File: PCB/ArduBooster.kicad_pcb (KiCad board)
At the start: 2 copper layers, 70.1 x 55.1 mm, 35 parts, among them IC1 ATMEGA328-P, P1 ISP, P2 DEBUG TX/RX, P3 CONTROL, P4 MAIN_CONN, U1 ICL7660, U2 LM358, U3 4052, X1 CRYSTAL

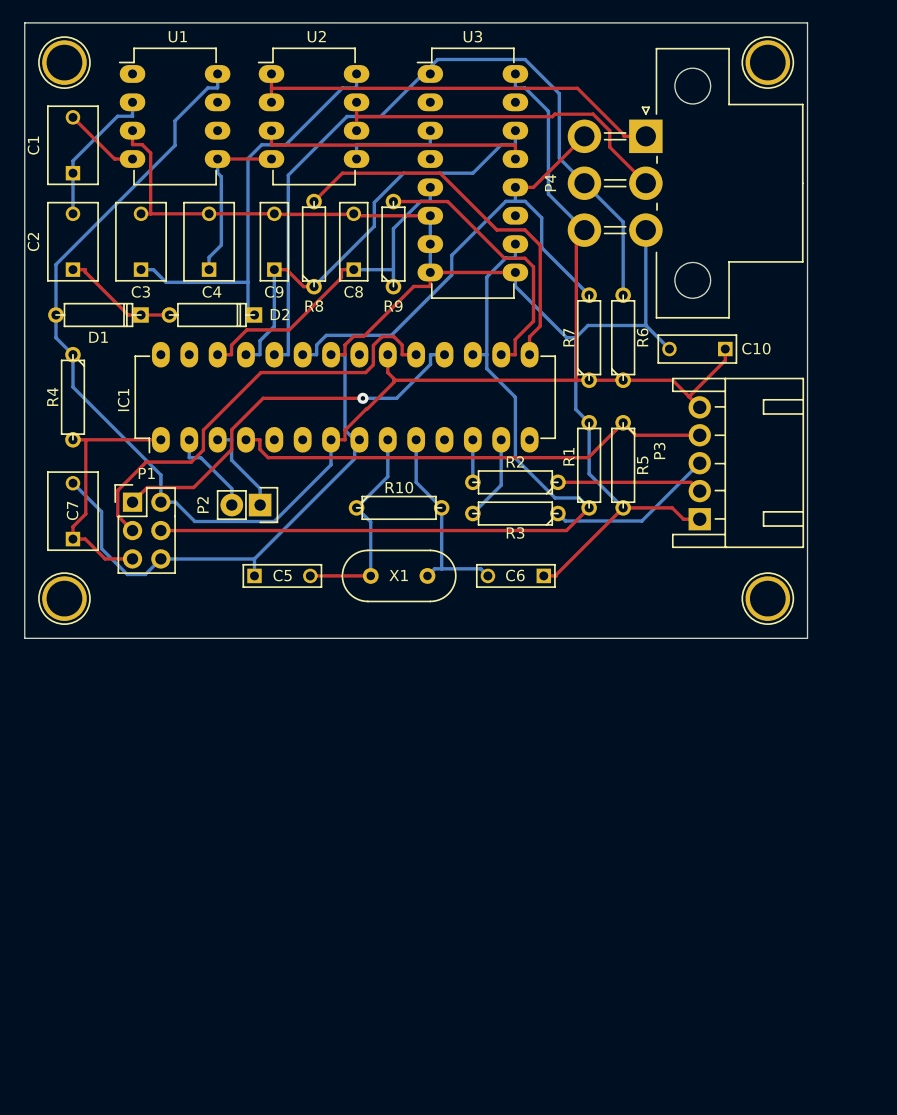
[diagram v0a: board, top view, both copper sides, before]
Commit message: New route, gerber files and drill files.
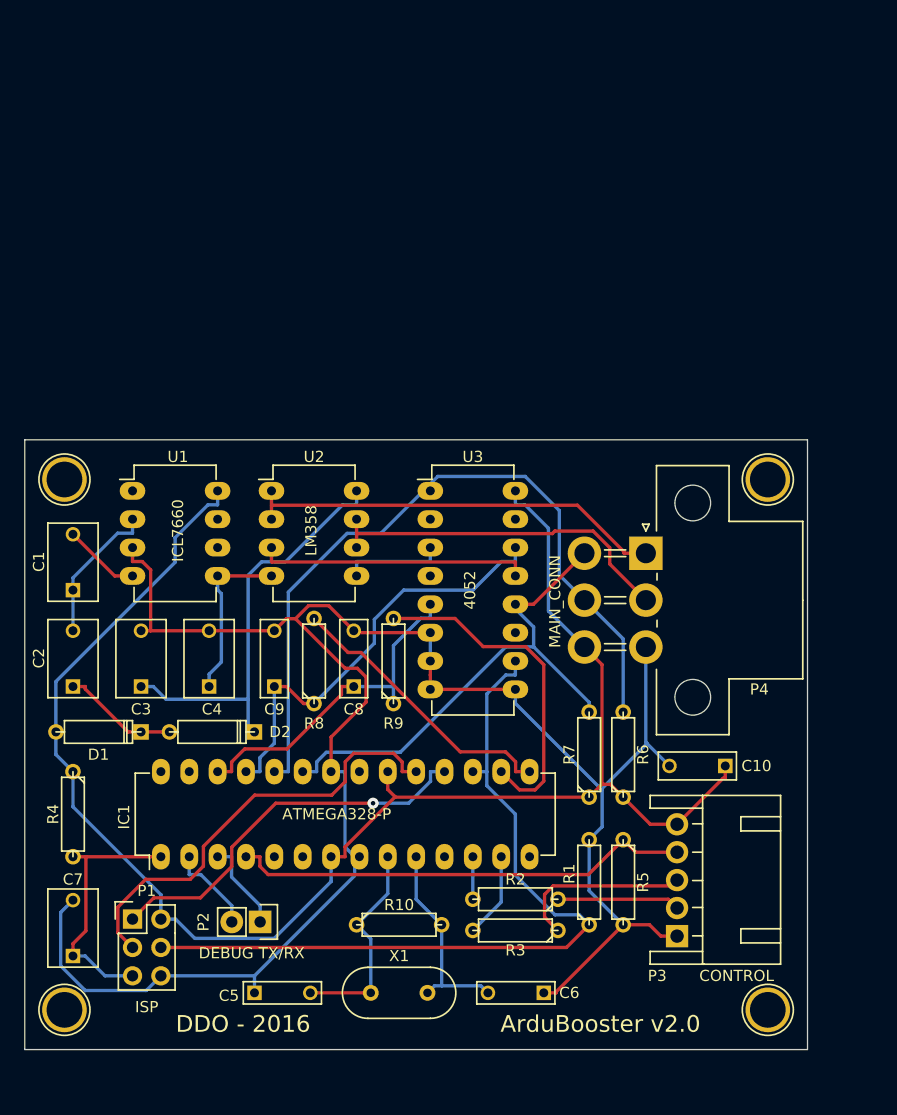
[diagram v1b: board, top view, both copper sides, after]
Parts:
- moved P3 37.4 mm to (168.9, 118.6)
- moved C2 37.3 mm to (114.8, 96.3)
- moved C3 37.3 mm to (120.9, 96.3)
- moved C4 37.3 mm to (127.0, 96.3)
- moved C8 37.3 mm to (140.0, 96.3)
- moved C9 37.3 mm to (132.8, 96.3)
- moved R1 37.3 mm to (161.0, 113.8)
- moved R10 37.3 mm to (144.0, 117.6)
- moved R2 37.3 mm to (154.4, 115.3)
- moved R5 37.3 mm to (164.1, 113.8)
- moved D1 37.3 mm to (117.1, 100.3)
- moved D2 37.3 mm to (127.3, 100.3)
- moved H1 37.3 mm to (177.0, 77.7)
- moved H3 37.3 mm to (114.0, 77.7)
- moved P4 37.3 mm to (166.1, 84.3)
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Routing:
- net Net-(IC1-Pad15): track 34.2 -> 25.5 mm
- net GNDREF: track 169.0 -> 176.4 mm
- net Net-(IC1-Pad16): track 24.8 -> 30.4 mm
- net /Base Arduino/LED1: track 13.0 -> 11.0 mm
- net /Base Arduino/SWITCH: track 43.6 -> 41.5 mm
- net /Base Arduino/LED2: track 15.1 -> 16.1 mm
- net /Base Arduino/CH0_PEDAL_SIG: track 47.2 -> 46.3 mm
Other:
- board size 70.1 x 55.1 mm -> 70.1 x 54.6 mm
- board text added: "ArduBooster v2.0"
- board text added: "DDO - 2016"
- board text added: "www.github.com/ddo02/ArduBooster"

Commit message: Output feedback connection  correction.
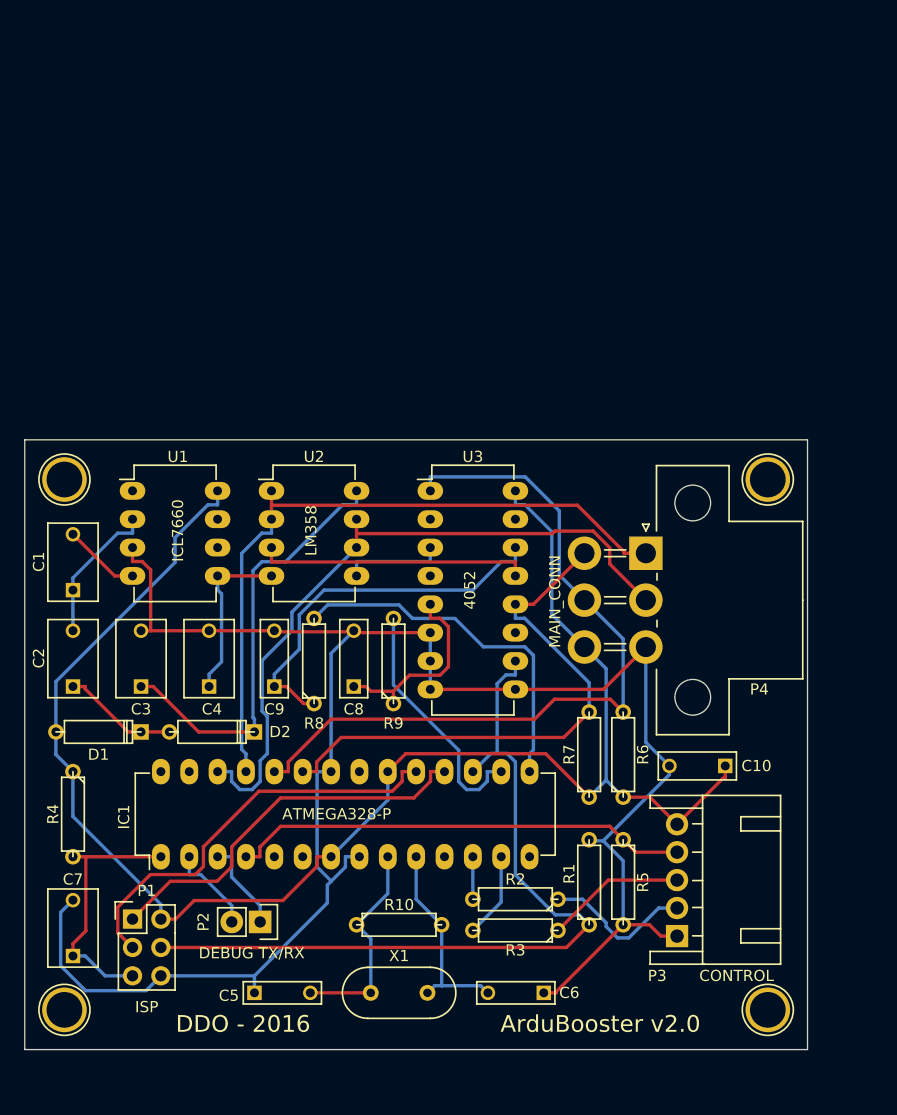
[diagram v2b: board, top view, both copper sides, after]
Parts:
- C10: value 100n -> 100nF
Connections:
- IC1 pad 25: /Base Arduino/CH0_ARDUINO_SIG -> /Base Arduino/CH0_OUT
- IC1 pad 26: /Base Arduino/CH1_ARDUINO_SIG -> /Base Arduino/CH1_OUT
- P4 pad 1: /Connectors/CH0_OUT -> /Base Arduino/CH0_OUT
- P4 pad 2: /Connectors/CH1_OUT -> /Base Arduino/CH1_OUT
- U2 pad 1: /Connectors/CH0_OUT -> /Base Arduino/CH0_OUT
- U2 pad 2: /Connectors/CH0_OUT -> /Base Arduino/CH0_OUT
- U2 pad 6: /Connectors/CH1_OUT -> /Base Arduino/CH1_OUT
- U2 pad 7: /Connectors/CH1_OUT -> /Base Arduino/CH1_OUT
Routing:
- net /Base Arduino/CH0_OUT: track 0.00 -> 62.3 mm
- net /Base Arduino/CH1_OUT: track 0.00 -> 62.2 mm
- net /Connectors/CH0_OUT: track 37.9 -> 0.00 mm
- net /Connectors/CH1_OUT: track 32.0 -> 0.00 mm
- net /Base Arduino/CH1_ARDUINO_SIG: track 30.6 -> 17.4 mm
- net Net-(IC1-Pad16): track 30.4 -> 22.3 mm
- net Net-(IC1-Pad15): track 25.5 -> 32.6 mm
- net /Base Arduino/CH0_ARDUINO_SIG: track 39.4 -> 34.1 mm
- net /Base Arduino/LED2: track 16.1 -> 12.5 mm
- net GNDREF: track 176.4 -> 172.9 mm
- net /Base Arduino/CH0_PEDAL_SIG: track 46.3 -> 49.3 mm
- net /Base Arduino/LED1: track 11.0 -> 13.4 mm
- net /Base Arduino/SCK: track 39.8 -> 37.4 mm
- net /Base Arduino/MOSI: track 70.7 -> 72.0 mm
- net /Base Arduino/CH1_PEDAL_SIG: track 68.2 -> 69.4 mm
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
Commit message: Last commit before Mux/Demux removel. Single layer PCB incompete (3 wires). Add ADC input filter.
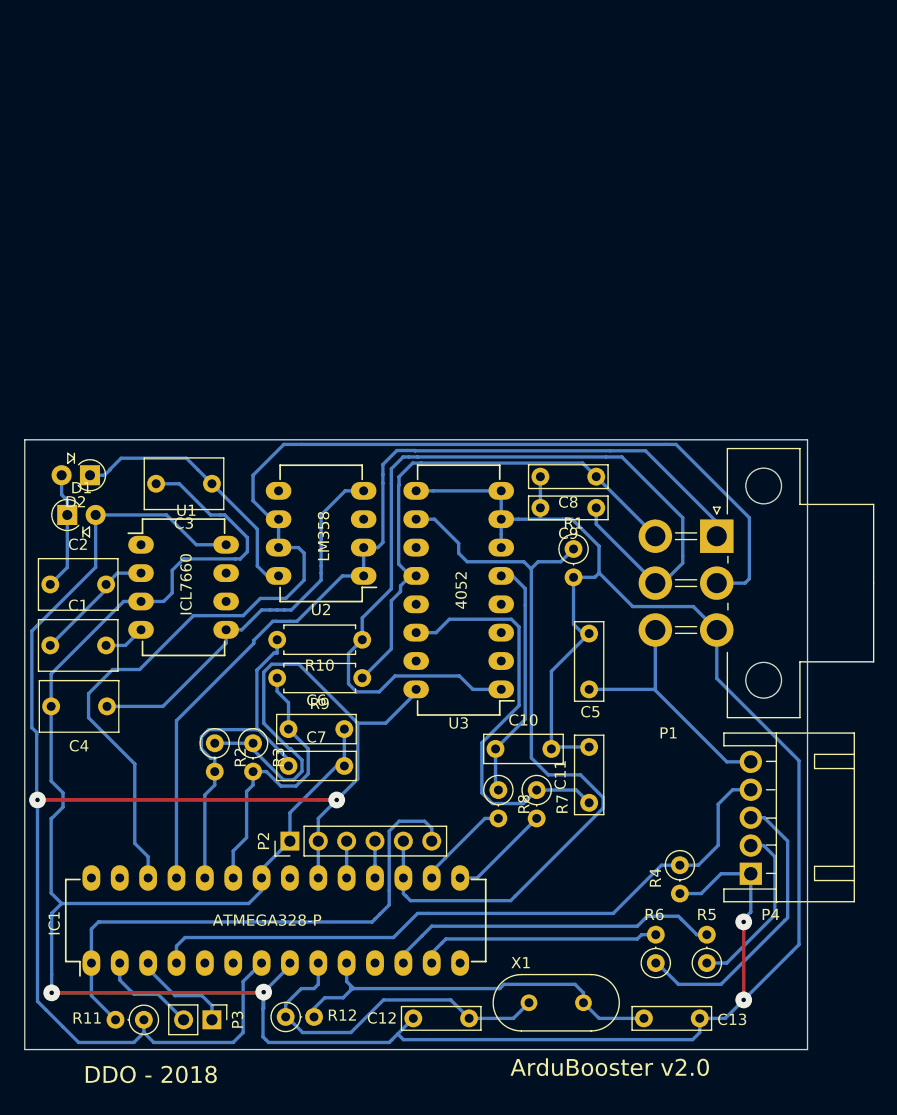
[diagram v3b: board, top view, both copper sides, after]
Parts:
- removed H1, H2, H3, H4: , Connect:1pin
- added C11: 100n, Capacitors_THT:C_Rect_L7.0mm_W2.5mm_P5.00mm, F.Cu at (161.0, 106.7)
- added C12: 22p, Capacitors_THT:C_Rect_L7.0mm_W2.0mm_P5.00mm, F.Cu at (145.3, 126.0)
- added C13: 22p, Capacitors_THT:C_Rect_L7.0mm_W2.0mm_P5.00mm, F.Cu at (170.9, 126.0)
- added R11: 10k, Resistors_THT:R_Axial_DIN0207_L6.3mm_D2.5mm_P2.54mm_Vertical, F.Cu at (121.2, 126.1)
- added R12: 1M, Resistors_THT:R_Axial_DIN0207_L6.3mm_D2.5mm_P2.54mm_Vertical, F.Cu at (133.9, 125.9)
- C1, C2, C3, C4: footprint Capacitors_ThroughHole:C_Rect_L7_W4.5_P5 -> Capacitors_THT:C_Rect_L7.0mm_W4.5mm_P5.00mm
- C10: value 100nF -> 100n; footprint Capacitors_ThroughHole:C_Rect_L7_W2.5_P5 -> Capacitors_THT:C_Rect_L7.0mm_W2.5mm_P5.00mm
- C5: value 22p -> 100nF; footprint Capacitors_ThroughHole:C_Rect_L7_W2_P5 -> Capacitors_THT:C_Rect_L7.0mm_W2.5mm_P5.00mm
- C6: value 22p -> 100n; footprint Capacitors_ThroughHole:C_Rect_L7_W2_P5 -> Capacitors_THT:C_Rect_L7.0mm_W2.5mm_P5.00mm
- C7: value 1u -> 100n; footprint Capacitors_ThroughHole:C_Rect_L7_W4.5_P5 -> Capacitors_THT:C_Rect_L7.0mm_W2.5mm_P5.00mm
- C8, C9: value 100n -> 1n; footprint Capacitors_ThroughHole:C_Rect_L7_W2.5_P5 -> Capacitors_THT:C_Rect_L7.0mm_W2.0mm_P5.00mm
- D1, D2: footprint Discret:D3 -> Diodes_THT:D_A-405_P2.54mm_Vertical_AnodeUp
- P1: value ISP -> MAIN_CONN; footprint Pin_Headers:Pin_Header_Straight_2x03 -> Connectors_Molex:Molex_MiniFit-JR-5569-06A1_2x03x4.20mm_Angled
- P2: value DEBUG TX/RX -> ISP; footprint Pin_Headers:Pin_Header_Straight_1x02 -> Pin_Headers:Pin_Header_Straight_1x06_Pitch2.54mm
- P3: value CONTROL -> DEBUG TX/RX; footprint Connect:Wafer_Horizontal15x5.8x7RM2.5-5 -> Pin_Headers:Pin_Header_Straight_1x02_Pitch2.54mm
- P4: value MAIN_CONN -> CONTROL; footprint Connectors_Molex:Molex_MiniFit-JR-5569-06A1_2x03x4.20mm_Angled -> Connectors:Wafer_Horizontal15x5.8x7RM2.5-5
- R1, R4: footprint Discret:R3 -> Resistors_THT:R_Axial_DIN0207_L6.3mm_D2.5mm_P2.54mm_Vertical
- R10: value 1M -> 2.2k; footprint Discret:R3 -> Resistors_THT:R_Axial_DIN0207_L6.3mm_D2.5mm_P7.62mm_Horizontal
- R2, R3: value 470 -> 10k; footprint Discret:R3 -> Resistors_THT:R_Axial_DIN0207_L6.3mm_D2.5mm_P2.54mm_Vertical
- R5, R6: value 10k -> 470; footprint Discret:R3 -> Resistors_THT:R_Axial_DIN0207_L6.3mm_D2.5mm_P2.54mm_Vertical
- R7, R8: value 10k -> 100k; footprint Discret:R3 -> Resistors_THT:R_Axial_DIN0207_L6.3mm_D2.5mm_P2.54mm_Vertical
- R9: value 10k -> 2.2k; footprint Discret:R3 -> Resistors_THT:R_Axial_DIN0207_L6.3mm_D2.5mm_P7.62mm_Horizontal
- X1: footprint Crystals:HC-49V -> Crystals:Crystal_HC49-U_Vertical
- moved P1 62.6 mm to (172.5, 82.8), turned to 270 degrees
- moved R4 54.5 mm to (169.2, 112.3)
- moved P3 42.3 mm to (127.3, 126.1), turned to 270 degrees
- moved C5 40.5 mm to (161.0, 96.5), turned to 90 degrees
- moved C9 33.0 mm to (161.7, 80.3), turned to 180 degrees
- moved C6 32.9 mm to (134.1, 100.1), turned to 0 degrees
- moved R2 30.3 mm to (127.5, 101.3), turned to 270 degrees
- moved P4 30.2 mm to (175.5, 113.0), turned to 90 degrees
- moved R1 29.9 mm to (159.6, 83.9), turned to 270 degrees
- moved R3 28.9 mm to (130.9, 101.3), turned to 270 degrees
- moved C8 28.7 mm to (161.7, 77.5), turned to 180 degrees
- moved R10 25.7 mm to (140.7, 92.1), turned to 180 degrees
- moved C7 25.7 mm to (134.1, 103.4), turned to 0 degrees
- moved D2 25.4 mm to (116.3, 77.3), turned to 180 degrees
- moved C10 20.6 mm to (152.7, 101.9), turned to 0 degrees
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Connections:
- C10 pad 1: +5V -> /Base Arduino/CH1_ARDUINO_SIG
- C5 pad 1: GNDREF -> +5V
- C5 pad 2: Net-(C5-Pad2) -> GNDREF
- C6 pad 1: GNDREF -> Net-(C6-Pad1)
- C6 pad 2: Net-(C6-Pad2) -> GNDREF
- C7 pad 1: /Base Arduino/RESET -> Net-(C7-Pad1)
- C8 pad 1: /Base Arduino/CH1_ARDUINO_SIG -> /Base Arduino/CH0_PEDAL_SIG
- C9 pad 1: /Base Arduino/CH0_ARDUINO_SIG -> /Base Arduino/CH1_PEDAL_SIG
- IC1 pad 10: Net-(C6-Pad2) -> Net-(C13-Pad2)
- IC1 pad 11: Net-(IC1-Pad11) -> (no net)
- IC1 pad 14: Net-(IC1-Pad14) -> (no net)
- IC1 pad 21: Net-(IC1-Pad21) -> (no net)
- IC1 pad 23: /Base Arduino/CH0_PEDAL_SIG -> Net-(C6-Pad1)
- IC1 pad 24: /Base Arduino/CH1_PEDAL_SIG -> Net-(C7-Pad1)
- IC1 pad 27: Net-(IC1-Pad27) -> (no net)
- IC1 pad 28: Net-(IC1-Pad28) -> (no net)
- IC1 pad 5: Net-(IC1-Pad5) -> (no net)
- IC1 pad 6: Net-(IC1-Pad6) -> (no net)
- IC1 pad 9: Net-(C5-Pad2) -> Net-(C12-Pad2)
- P1 pad 1: /Base Arduino/MISO -> /Base Arduino/CH0_OUT
- P1 pad 2: +5V -> /Base Arduino/CH1_OUT
- P1 pad 3: /Base Arduino/SCK -> GNDREF
- P1 pad 4: /Base Arduino/MOSI -> /Base Arduino/CH0_PEDAL_SIG
- P1 pad 5: /Base Arduino/RESET -> /Base Arduino/CH1_PEDAL_SIG
- P1 pad 6: GNDREF -> +5V
- P2 pad 1: /Base Arduino/TX -> GNDREF
- P2 pad 2: /Base Arduino/RX -> +5V
- P3 pad 1: GNDREF -> /Base Arduino/TX
- P3 pad 2: /Base Arduino/LED1 -> /Base Arduino/RX
- P4 pad 1: /Base Arduino/CH0_OUT -> GNDREF
- P4 pad 2: /Base Arduino/CH1_OUT -> /Base Arduino/LED1
- P4 pad 3: GNDREF -> /Base Arduino/LED2
- P4 pad 4: /Base Arduino/CH0_PEDAL_SIG -> /Base Arduino/SWITCH
- P4 pad 5: /Base Arduino/CH1_PEDAL_SIG -> +5V
- R10 pad 1: Net-(C5-Pad2) -> /Base Arduino/CH1_PEDAL_SIG
- R10 pad 2: Net-(C6-Pad2) -> Net-(C7-Pad1)
- R2 pad 1: /Base Arduino/LED1 -> +5V
- R2 pad 2: Net-(IC1-Pad12) -> Net-(C7-Pad1)
- R3 pad 1: /Base Arduino/LED2 -> +5V
- R3 pad 2: Net-(IC1-Pad13) -> Net-(C6-Pad1)
- R4 pad 1: +5V -> /Base Arduino/SWITCH
- R4 pad 2: /Base Arduino/RESET -> GNDREF
- R5 pad 1: /Base Arduino/SWITCH -> /Base Arduino/LED1
- R5 pad 2: GNDREF -> Net-(IC1-Pad12)
- R6 pad 1: +5V -> /Base Arduino/LED2
- R6 pad 2: /Base Arduino/CH1_PEDAL_SIG -> Net-(IC1-Pad13)
- R7 pad 1: +5V -> /Base Arduino/CH0_ARDUINO_SIG
- R7 pad 2: /Base Arduino/CH0_PEDAL_SIG -> Net-(IC1-Pad15)
- R8 pad 1: /Base Arduino/CH0_ARDUINO_SIG -> /Base Arduino/CH1_ARDUINO_SIG
- R8 pad 2: Net-(IC1-Pad15) -> Net-(IC1-Pad16)
- R9 pad 1: /Base Arduino/CH1_ARDUINO_SIG -> /Base Arduino/CH0_PEDAL_SIG
- R9 pad 2: Net-(IC1-Pad16) -> Net-(C6-Pad1)
- U1 pad 6: Net-(U1-Pad6) -> (no net)
- U1 pad 7: Net-(U1-Pad7) -> (no net)
- U3 pad 11: Net-(U3-Pad11) -> (no net)
- U3 pad 15: Net-(U3-Pad15) -> (no net)
- U3 pad 2: Net-(U3-Pad2) -> (no net)
- U3 pad 4: Net-(U3-Pad4) -> (no net)
- X1 pad 1: Net-(C6-Pad2) -> Net-(C13-Pad2)
- X1 pad 2: Net-(C5-Pad2) -> Net-(C12-Pad2)
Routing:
- net GNDREF: track 172.9 -> 299.8 mm, vias 0 -> 4
- net /Base Arduino/CH1_OUT: track 62.2 -> 111.8 mm
- net +5V: track 143.9 -> 190.6 mm, vias 0 -> 2
- net Net-(C13-Pad2): track 0.00 -> 36.1 mm
- net /Base Arduino/SCK: track 37.4 -> 3.30 mm
- net Net-(C7-Pad1): track 0.00 -> 32.4 mm
- net Net-(C12-Pad2): track 0.00 -> 31.5 mm
- net /Base Arduino/MISO: track 35.0 -> 4.45 mm
- net /Base Arduino/RESET: track 23.3 -> 49.8 mm
- net Net-(IC1-Pad12): track 3.81 -> 30.0 mm
- net Net-(C6-Pad1): track 0.00 -> 25.9 mm
- net /Isolator/CH0_MUXDEMUX_OUT: track 24.4 -> 0.00 mm
- net Net-(IC1-Pad15): track 32.6 -> 9.07 mm
- net /Doubler_Inverter/-5V: track 15.3 -> 36.1 mm
- net /Base Arduino/CH0_OUT: track 62.3 -> 82.2 mm
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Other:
- net class Default: clearance 0.3 -> 0.25; via_dia 1 -> 1.5
- net class jumper added: clearance 0.1, trace_width 0.1, via_dia 1, via_drill 0.4
- rule trace_clearance: 0.3 -> 0.25
- rule trace_min: 0.254 -> 0.1
- board text added: "DDO - 2018"
- board text removed: "DDO - 2016"
